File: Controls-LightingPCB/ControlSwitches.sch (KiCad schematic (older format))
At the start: 13 parts, among them J6 Backup, SW1 HAZARD, SW2 CRUISE_SET, SW3 CRUISE, SW4 F/R_SW, SW5 HEADLIGHT_SW, SW6 BACKUP_SW, SW7 TURN_SIGNAL_SW

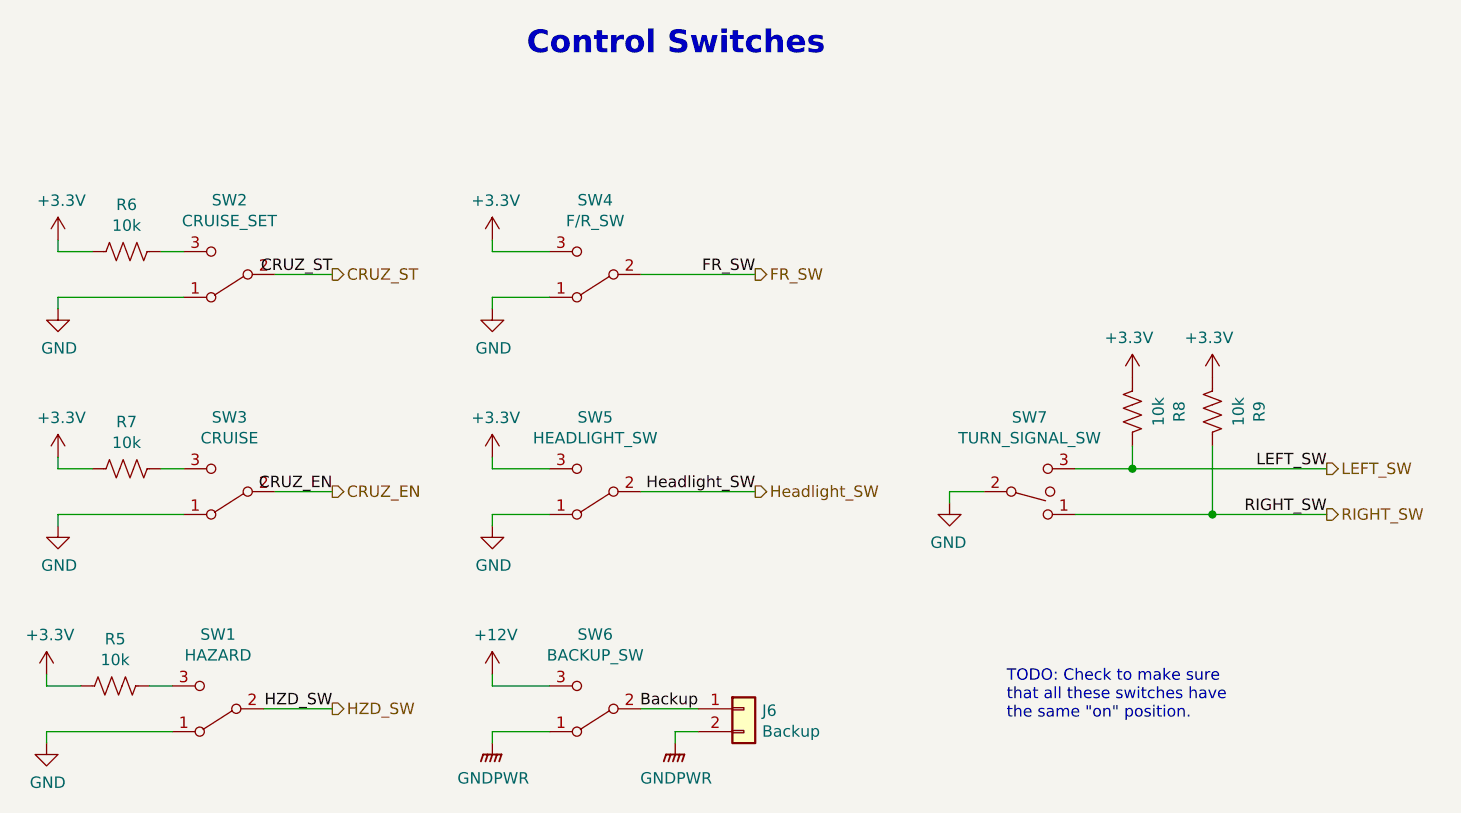
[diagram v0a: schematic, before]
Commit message: Added hierarchical sheets and connections
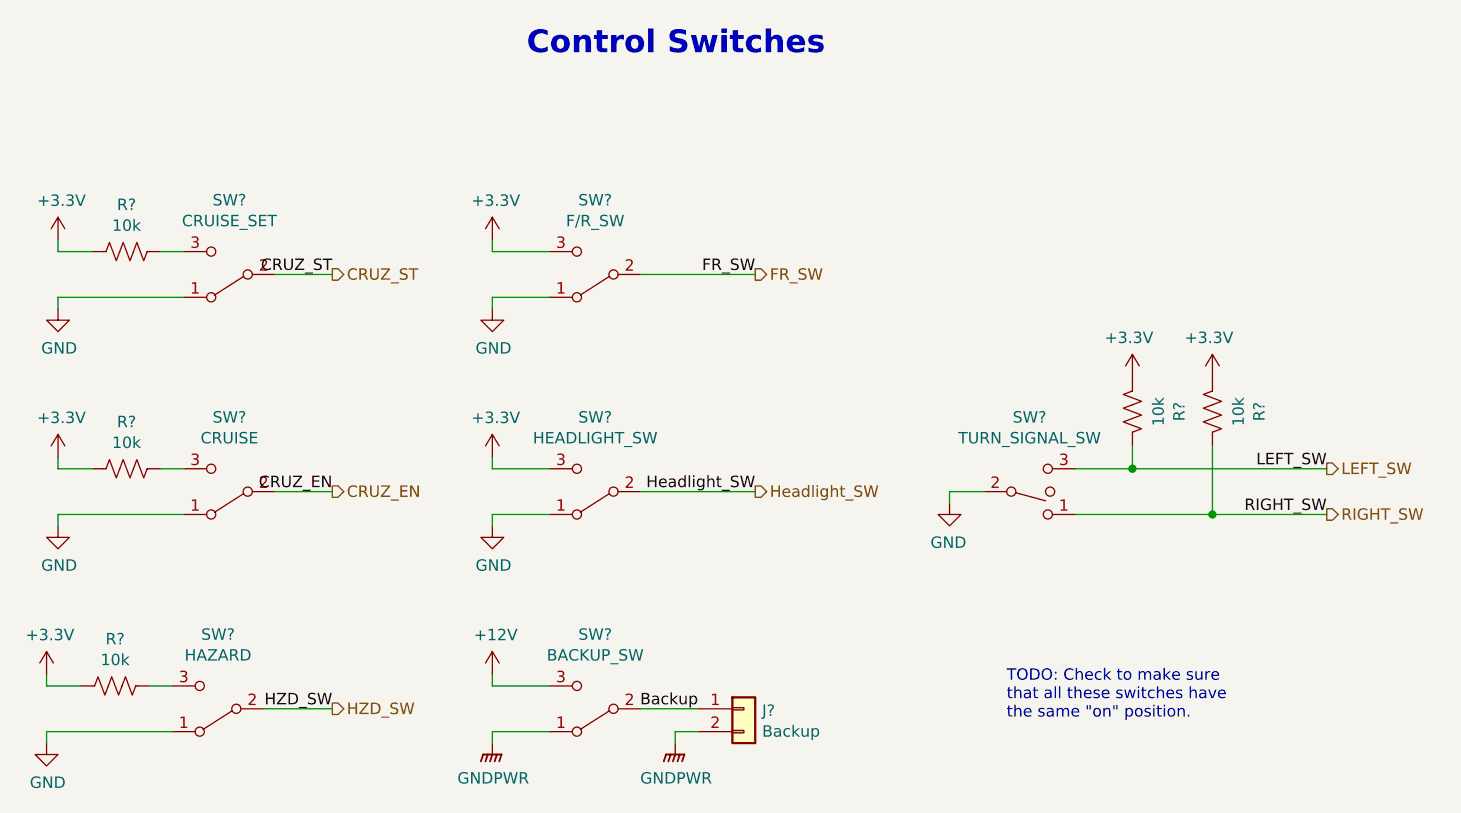
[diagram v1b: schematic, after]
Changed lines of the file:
@@
 $Descr A4 11693 8268
 encoding utf-8
-Sheet 7 10
+Sheet 7 4
 Title ""
 Date ""
@@
 AR Path="/5F95FCE0" Ref="SW?"  Part="1"
 AR Path="/5F958945/5F95FCE0" Ref="SW2"  Part="1"
-F 0 "SW2" H 4000 2875 50  0000 C CNN
+F 0 "SW?" H 4000 2875 50  0000 C CNN
 F 1 "CRUISE_SET" H 4000 2966 50  0000 C CNN
 F 2 "UTSVT_Connectors:Molex_MicroFit3.0_1x3xP3.00mm_PolarizingPeg_Vertical" H 4000 3200 50  0001 C CNN
@@
 AR Path="/5F95FCE7" Ref="R?"  Part="1"
 AR Path="/5F958945/5F95FCE7" Ref="R6"  Part="1"
-F 0 "R6" V 3345 3100 50  0000 C CNN
+F 0 "R?" V 3345 3100 50  0000 C CNN
 F 1 "10k" V 3436 3100 50  0000 C CNN
 F 2 "Resistor_SMD:R_0805_2012Metric" V 3590 3090 50  0001 C CNN
@@
 AR Path="/5F95FCED" Ref="#PWR?"  Part="1"
 AR Path="/5F958945/5F95FCED" Ref="#PWR0127"  Part="1"
-F 0 "#PWR0127" H 3250 2900 50  0001 C CNN
+F 0 "#PWR?" H 3250 2900 50  0001 C CNN
 F 1 "+3.3V" H 3265 3223 50  0000 C CNN
 F 2 "" H 3250 3050 50  0001 C CNN
@@
 AR Path="/5F95FCF6" Ref="#PWR?"  Part="1"
 AR Path="/5F958945/5F95FCF6" Ref="#PWR0128"  Part="1"
-F 0 "#PWR0128" H 3250 3100 50  0001 C CNN
+F 0 "#PWR?" H 3250 3100 50  0001 C CNN
 F 1 "GND" H 3255 3177 50  0000 C CNN
 F 2 "" H 3250 3350 50  0001 C CNN
@@
 AR Path="/5F95FCFE" Ref="SW?"  Part="1"
 AR Path="/5F958945/5F95FCFE" Ref="SW3"  Part="1"
-F 0 "SW3" H 4000 3825 50  0000 C CNN
+F 0 "SW?" H 4000 3825 50  0000 C CNN
 F 1 "CRUISE" H 4000 3916 50  0000 C CNN
 F 2 "UTSVT_Connectors:Molex_MicroFit3.0_1x3xP3.00mm_PolarizingPeg_Vertical" H 4000 4150 50  0001 C CNN
@@
 AR Path="/5F95FD05" Ref="R?"  Part="1"
 AR Path="/5F958945/5F95FD05" Ref="R7"  Part="1"
-F 0 "R7" V 3345 4050 50  0000 C CNN
+F 0 "R?" V 3345 4050 50  0000 C CNN
 F 1 "10k" V 3436 4050 50  0000 C CNN
 F 2 "Resistor_SMD:R_0805_2012Metric" V 3590 4040 50  0001 C CNN
@@
 AR Path="/5F95FD0B" Ref="#PWR?"  Part="1"
 AR Path="/5F958945/5F95FD0B" Ref="#PWR0129"  Part="1"
-F 0 "#PWR0129" H 3250 3850 50  0001 C CNN
+F 0 "#PWR?" H 3250 3850 50  0001 C CNN
 F 1 "+3.3V" H 3265 4173 50  0000 C CNN
 F 2 "" H 3250 4000 50  0001 C CNN
@@
 AR Path="/5F95FD14" Ref="#PWR?"  Part="1"
 AR Path="/5F958945/5F95FD14" Ref="#PWR0130"  Part="1"
-F 0 "#PWR0130" H 3250 4050 50  0001 C CNN
+F 0 "#PWR?" H 3250 4050 50  0001 C CNN
 F 1 "GND" H 3255 4127 50  0000 C CNN
 F 2 "" H 3250 4300 50  0001 C CNN
@@
 AR Path="/5F95FD1C" Ref="SW?"  Part="1"
 AR Path="/5F958945/5F95FD1C" Ref="SW1"  Part="1"
-F 0 "SW1" H 3950 4775 50  0000 C CNN
+F 0 "SW?" H 3950 4775 50  0000 C CNN
 F 1 "HAZARD" H 3950 4866 50  0000 C CNN
 F 2 "UTSVT_Connectors:Molex_MicroFit3.0_1x3xP3.00mm_PolarizingPeg_Vertical" H 3950 5100 50  0001 C CNN
@@
 AR Path="/5F95FD23" Ref="R?"  Part="1"
 AR Path="/5F958945/5F95FD23" Ref="R5"  Part="1"
-F 0 "R5" V 3295 5000 50  0000 C CNN
+F 0 "R?" V 3295 5000 50  0000 C CNN
 F 1 "10k" V 3386 5000 50  0000 C CNN
 F 2 "Resistor_SMD:R_0805_2012Metric" V 3540 4990 50  0001 C CNN
@@
 AR Path="/5F95FD29" Ref="#PWR?"  Part="1"
 AR Path="/5F958945/5F95FD29" Ref="#PWR0131"  Part="1"
-F 0 "#PWR0131" H 3200 4800 50  0001 C CNN
+F 0 "#PWR?" H 3200 4800 50  0001 C CNN
 F 1 "+3.3V" H 3215 5123 50  0000 C CNN
 F 2 "" H 3200 4950 50  0001 C CNN
@@
 AR Path="/5F95FD32" Ref="#PWR?"  Part="1"
 AR Path="/5F958945/5F95FD32" Ref="#PWR0132"  Part="1"
-F 0 "#PWR0132" H 3200 5000 50  0001 C CNN
+F 0 "#PWR?" H 3200 5000 50  0001 C CNN
 F 1 "GND" H 3205 5077 50  0000 C CNN
 F 2 "" H 3200 5250 50  0001 C CNN
@@
 AR Path="/5F95FD3D" Ref="SW?"  Part="1"
 AR Path="/5F958945/5F95FD3D" Ref="SW7"  Part="1"
-F 0 "SW7" H 7500 3825 50  0000 C CNN
+F 0 "SW?" H 7500 3825 50  0000 C CNN
 F 1 "TURN_SIGNAL_SW" H 7500 3916 50  0000 C CNN
 F 2 "UTSVT_Connectors:Molex_MicroFit3.0_1x3xP3.00mm_PolarizingPeg_Vertical" H 7500 4150 50  0001 C CNN
@@
 AR Path="/5F95FD47" Ref="#PWR?"  Part="1"
 AR Path="/5F958945/5F95FD47" Ref="#PWR0133"  Part="1"
-F 0 "#PWR0133" H 7150 3950 50  0001 C CNN
+F 0 "#PWR?" H 7150 3950 50  0001 C CNN
 F 1 "GND" H 7155 4027 50  0000 C CNN
 F 2 "" H 7150 4200 50  0001 C CNN
@@
 AR Path="/5F95FD4F" Ref="SW?"  Part="1"
 AR Path="/5F958945/5F95FD4F" Ref="SW4"  Part="1"
-F 0 "SW4" H 5600 2875 50  0000 C CNN
+F 0 "SW?" H 5600 2875 50  0000 C CNN
 F 1 "F/R_SW" H 5600 2966 50  0000 C CNN
 F 2 "UTSVT_Connectors:Molex_MicroFit3.0_1x3xP3.00mm_PolarizingPeg_Vertical" H 5600 3200 50  0001 C CNN
@@
 AR Path="/5F95FD55" Ref="#PWR?"  Part="1"
 AR Path="/5F958945/5F95FD55" Ref="#PWR0134"  Part="1"
-F 0 "#PWR0134" H 5150 2900 50  0001 C CNN
+F 0 "#PWR?" H 5150 2900 50  0001 C CNN
 F 1 "+3.3V" H 5165 3223 50  0000 C CNN
 F 2 "" H 5150 3050 50  0001 C CNN
@@
 AR Path="/5F95FD5C" Ref="#PWR?"  Part="1"
 AR Path="/5F958945/5F95FD5C" Ref="#PWR0135"  Part="1"
-F 0 "#PWR0135" H 5150 3100 50  0001 C CNN
+F 0 "#PWR?" H 5150 3100 50  0001 C CNN
 F 1 "GND" H 5155 3177 50  0000 C CNN
 F 2 "" H 5150 3350 50  0001 C CNN
@@
 AR Path="/5F95FD6B" Ref="SW?"  Part="1"
 AR Path="/5F958945/5F95FD6B" Ref="SW6"  Part="1"
-F 0 "SW6" H 5600 4775 50  0000 C CNN
+F 0 "SW?" H 5600 4775 50  0000 C CNN
 F 1 "BACKUP_SW" H 5600 4866 50  0000 C CNN
 F 2 "UTSVT_Connectors:Molex_MicroFit3.0_1x3xP3.00mm_PolarizingPeg_Vertical" H 5600 5100 50  0001 C CNN
@@
 AR Path="/5F95FD79" Ref="#PWR?"  Part="1"
 AR Path="/5F958945/5F95FD79" Ref="#PWR0136"  Part="1"
-F 0 "#PWR0136" H 5150 3850 50  0001 C CNN
+F 0 "#PWR?" H 5150 3850 50  0001 C CNN
 F 1 "+3.3V" H 5165 4173 50  0000 C CNN
 F 2 "" H 5150 4000 50  0001 C CNN
@@
 AR Path="/5F95FD81" Ref="#PWR?"  Part="1"
 AR Path="/5F958945/5F95FD81" Ref="#PWR0137"  Part="1"
-F 0 "#PWR0137" H 5150 4050 50  0001 C CNN
+F 0 "#PWR?" H 5150 4050 50  0001 C CNN
 F 1 "GND" H 5155 4127 50  0000 C CNN
 F 2 "" H 5150 4300 50  0001 C CNN
@@
 AR Path="/5F95FD88" Ref="SW?"  Part="1"
 AR Path="/5F958945/5F95FD88" Ref="SW5"  Part="1"
-F 0 "SW5" H 5600 3825 50  0000 C CNN
+F 0 "SW?" H 5600 3825 50  0000 C CNN
 F 1 "HEADLIGHT_SW" H 5600 3916 50  0000 C CNN
 F 2 "UTSVT_Connectors:Molex_MicroFit3.0_1x3xP3.00mm_PolarizingPeg_Vertical" H 5600 4150 50  0001 C CNN
@@
 AR Path="/5F95FD8F" Ref="J?"  Part="1"
 AR Path="/5F958945/5F95FD8F" Ref="J6"  Part="1"
-F 0 "J6" H 6330 5092 50  0000 L CNN
+F 0 "J?" H 6330 5092 50  0000 L CNN
 F 1 "Backup" H 6330 5001 50  0000 L CNN
 F 2 "UTSVT_Connectors:Molex_MicroFit3.0_1x2xP3.00mm_PolarizingPeg_Vertical" H 6250 5100 50  0001 C CNN
@@
 AR Path="/5F95FD95" Ref="#PWR?"  Part="1"
 AR Path="/5F958945/5F95FD95" Ref="#PWR0138"  Part="1"
-F 0 "#PWR0138" H 5950 5050 50  0001 C CNN
+F 0 "#PWR?" H 5950 5050 50  0001 C CNN
 F 1 "GNDPWR" H 5954 5096 50  0000 C CNN
 F 2 "" H 5950 5200 50  0001 C CNN
@@
 AR Path="/5F95FD9D" Ref="#PWR?"  Part="1"
 AR Path="/5F958945/5F95FD9D" Ref="#PWR0139"  Part="1"
-F 0 "#PWR0139" H 5150 5050 50  0001 C CNN
+F 0 "#PWR?" H 5150 5050 50  0001 C CNN
 F 1 "GNDPWR" H 5154 5096 50  0000 C CNN
 F 2 "" H 5150 5200 50  0001 C CNN
@@
 AR Path="/5F95FDA3" Ref="#PWR?"  Part="1"
 AR Path="/5F958945/5F95FDA3" Ref="#PWR0140"  Part="1"
-F 0 "#PWR0140" H 5150 4800 50  0001 C CNN
+F 0 "#PWR?" H 5150 4800 50  0001 C CNN
 F 1 "+12V" H 5165 5123 50  0000 C CNN
 F 2 "" H 5150 4950 50  0001 C CNN
@@
 AR Path="/5F95FDAA" Ref="R?"  Part="1"
 AR Path="/5F958945/5F95FDAA" Ref="R8"  Part="1"
-F 0 "R8" V 7745 3800 50  0000 C CNN
+F 0 "R?" V 7745 3800 50  0000 C CNN
 F 1 "10k" V 7836 3800 50  0000 C CNN
 F 2 "Resistor_SMD:R_0805_2012Metric" V 7990 3790 50  0001 C CNN
@@
 AR Path="/5F95FDB2" Ref="R?"  Part="1"
 AR Path="/5F958945/5F95FDB2" Ref="R9"  Part="1"
-F 0 "R9" V 8095 3800 50  0000 C CNN
+F 0 "R?" V 8095 3800 50  0000 C CNN
 F 1 "10k" V 8186 3800 50  0000 C CNN
 F 2 "Resistor_SMD:R_0805_2012Metric" V 8340 3790 50  0001 C CNN
@@
 AR Path="/5F95FDB8" Ref="#PWR?"  Part="1"
 AR Path="/5F958945/5F95FDB8" Ref="#PWR0141"  Part="1"
-F 0 "#PWR0141" H 8300 3500 50  0001 C CNN
+F 0 "#PWR?" H 8300 3500 50  0001 C CNN
 F 1 "+3.3V" H 8315 3823 50  0000 C CNN
 F 2 "" H 8300 3650 50  0001 C CNN
@@
 AR Path="/5F95FDBE" Ref="#PWR?"  Part="1"
 AR Path="/5F958945/5F95FDBE" Ref="#PWR0142"  Part="1"
-F 0 "#PWR0142" H 7950 3500 50  0001 C CNN
+F 0 "#PWR?" H 7950 3500 50  0001 C CNN
 F 1 "+3.3V" H 7965 3823 50  0000 C CNN
 F 2 "" H 7950 3650 50  0001 C CNN
